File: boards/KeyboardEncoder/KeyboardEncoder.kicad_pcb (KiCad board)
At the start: 2 copper layers, 19 parts, among them J1 ISP, J2 Encoder, J3 MIDI Out, J4 SelectRX, J5 MIDI In, J7 BoardCon, J8 PistonEncoder, U1 ATmega48-20P, U2 6N138

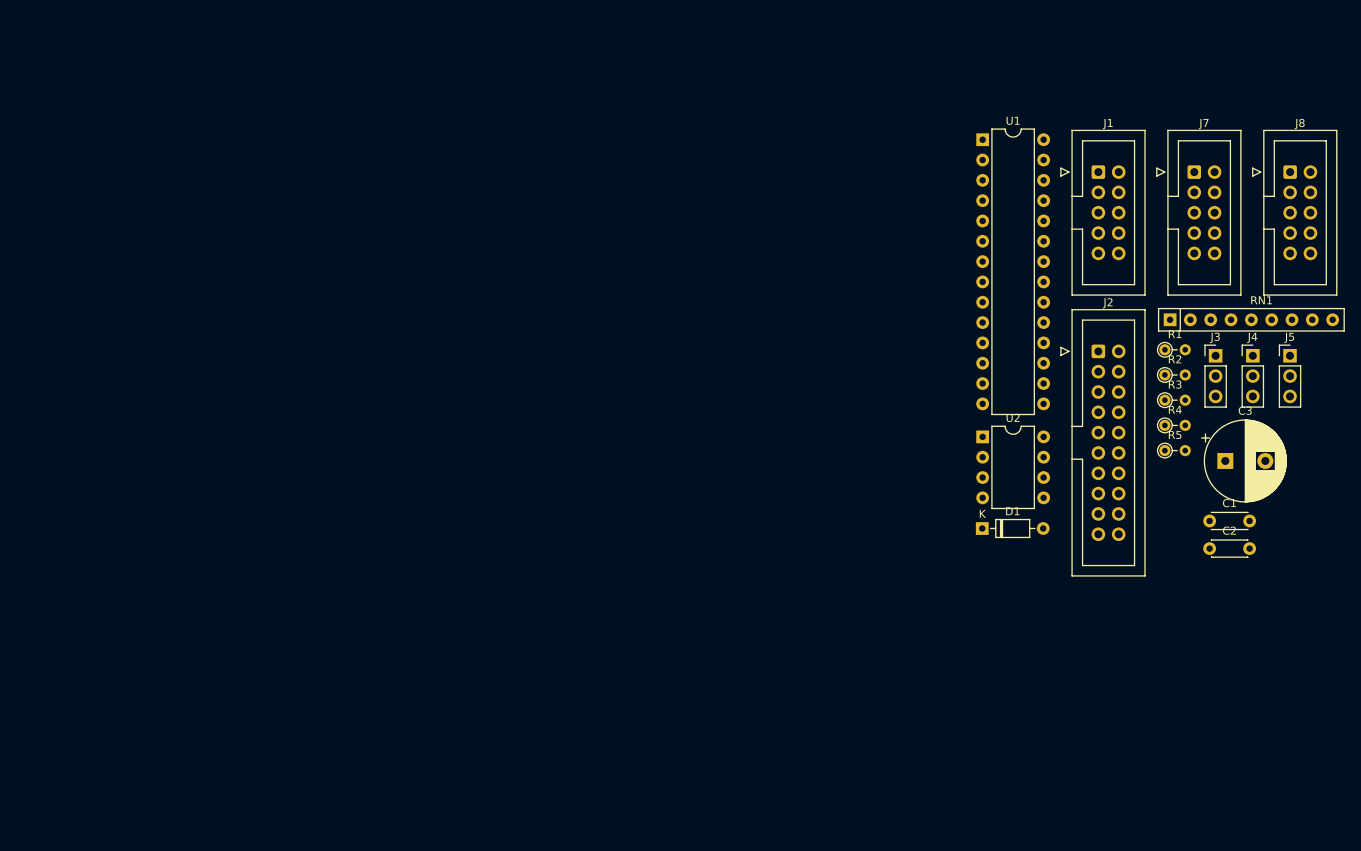
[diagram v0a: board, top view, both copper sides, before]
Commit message: Updated to KiCAD 8, fixed optocouplers for MIDI and added powersupplies
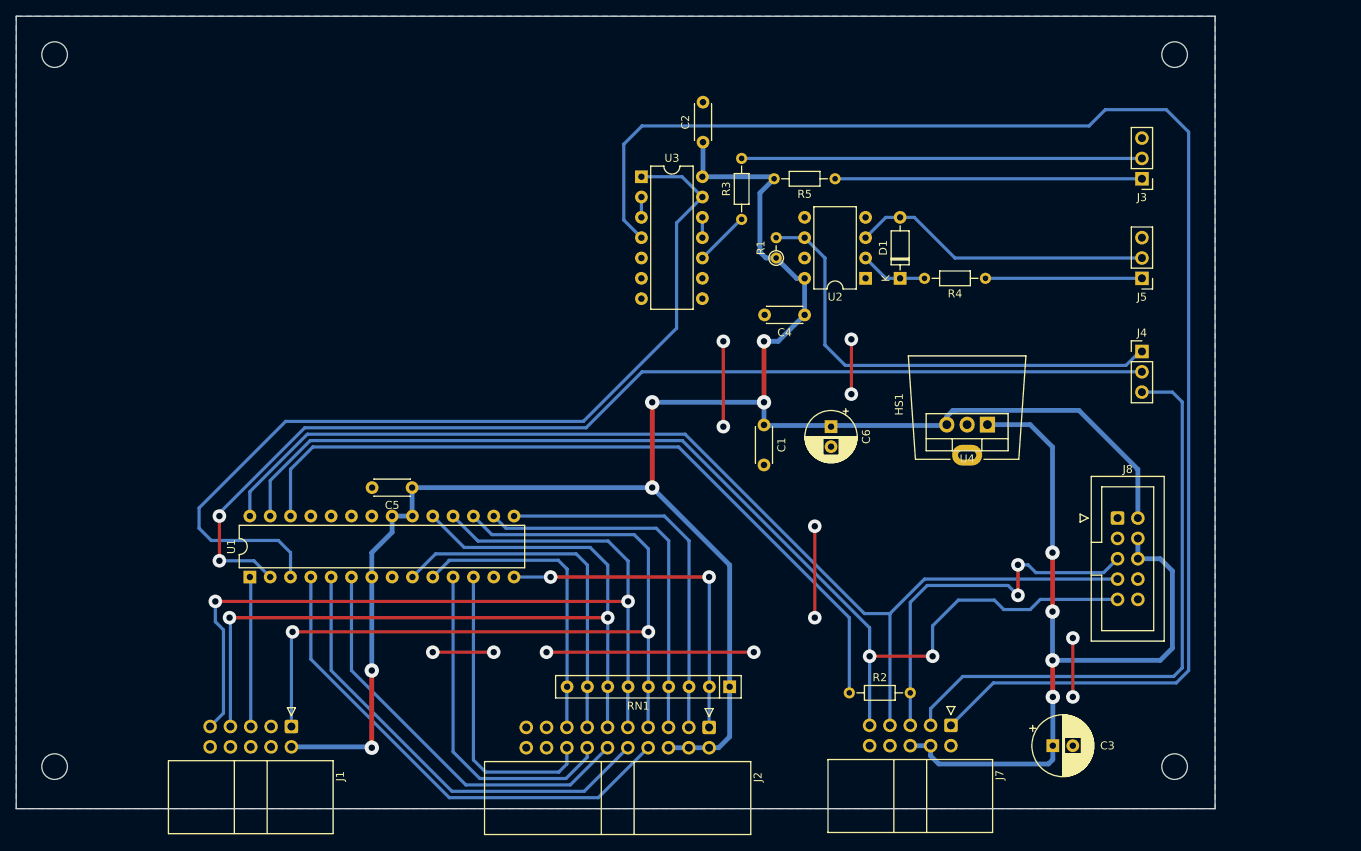
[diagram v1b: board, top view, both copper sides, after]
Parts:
- added C4: 100nF, Capacitor_THT:C_Disc_D4.3mm_W1.9mm_P5.00mm, F.Cu at (170.4, 82.5)
- added C5: 100nF, Capacitor_THT:C_Disc_D4.3mm_W1.9mm_P5.00mm, F.Cu at (121.4, 104.1)
- added C6: 10uF, Capacitor_THT:CP_Radial_D6.3mm_P2.50mm, F.Cu at (173.7, 96.5)
- added H1: MountingHole, MountingHole:MountingHole_3.2mm_M3, F.Cu at (216.7, 50.0)
- added H2: MountingHole, MountingHole:MountingHole_3.2mm_M3, F.Cu at (216.7, 139.0)
- added H3: MountingHole, MountingHole:MountingHole_3.2mm_M3, F.Cu at (76.7, 139.0)
- added H4: MountingHole, MountingHole:MountingHole_3.2mm_M3, F.Cu at (76.7, 50.0)
- added HS1: Heatsink_Pad, Heatsink:Heatsink_AAVID_576802B03900G, F.Cu at (190.7, 100.1)
- added U3: 74LS14, Package_DIP:DIP-14_W7.62mm, F.Cu at (150.0, 65.3)
- added U4: L7805, Package_TO_SOT_THT:TO-220-3_Vertical, F.Cu at (193.3, 96.3)
- C3: value C_Polarized -> 33uF; footprint Capacitor_THT:CP_Radial_D10.0mm_P5.00mm -> Capacitor_THT:CP_Radial_D7.5mm_P2.50mm
- J1, J7: footprint Connector_IDC:IDC-Header_2x05_P2.54mm_Vertical -> Connector_IDC:IDC-Header_2x05_P2.54mm_Horizontal
- J2: footprint Connector_IDC:IDC-Header_2x10_P2.54mm_Vertical -> Connector_IDC:IDC-Header_2x10_P2.54mm_Horizontal
- R1: value 10k -> 1k
- R2, R3, R4, R5: footprint Resistor_THT:R_Axial_DIN0204_L3.6mm_D1.6mm_P2.54mm_Vertical -> Resistor_THT:R_Axial_DIN0204_L3.6mm_D1.6mm_P7.62mm_Horizontal
- U2: value 6N138 -> 6N137
- moved J1 122.4 mm to (106.3, 134.0), turned to -90 degrees
- moved U1 106.7 mm to (101.1, 115.3), turned to 90 degrees
- moved C2 81.2 mm to (157.7, 61.0), turned to 90 degrees
- moved J7 75.6 mm to (188.7, 133.9), turned to -90 degrees
- moved RN1 71.7 mm to (161.1, 129.0), turned to 180 degrees
- moved J2 67.7 mm to (158.5, 134.1), turned to -90 degrees
- moved R3 57.5 mm to (162.6, 70.6), turned to 90 degrees
- moved C1 57.0 mm to (165.4, 96.3), turned to -90 degrees
- moved R2 56.0 mm to (176.0, 129.8)
- moved R5 53.4 mm to (174.2, 65.5), turned to 180 degrees
- moved R1 49.9 mm to (166.9, 75.4), turned to 90 degrees
- moved J8 48.3 mm to (209.6, 108.0)
- moved C3 41.6 mm to (201.5, 136.4)
- moved D1 32.9 mm to (182.4, 78.0), turned to 90 degrees
- moved R4 29.0 mm to (193.0, 78.0), turned to 180 degrees
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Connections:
- C3 pad 1: +5V -> +12V
- J7 pad 1: TXD -> TXT_OUT
- J7 pad 2: +5V -> unconnected-(J7-Pin_2-Pad2)
- R3 pad 1: TXD -> Net-(R3-Pad1)
- RN1 pad 2: Net-(J2-Pin_15) -> Net-(J2-Pin_1)
- RN1 pad 3: Net-(J2-Pin_13) -> Net-(J2-Pin_3)
- RN1 pad 4: SCK -> Net-(J2-Pin_5)
- RN1 pad 5: MISO -> MOSI
- RN1 pad 6: MOSI -> MISO
- RN1 pad 7: Net-(J2-Pin_5) -> SCK
- RN1 pad 8: Net-(J2-Pin_3) -> Net-(J2-Pin_13)
- RN1 pad 9: Net-(J2-Pin_1) -> Net-(J2-Pin_15)
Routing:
- net +5V: track 0.00 -> 253.2 mm, vias 0 -> 6
- net TXT_OUT: track 0.00 -> 186.0 mm
- net SDA: track 0.00 -> 140.5 mm, vias 0 -> 2
- net SCL: track 0.00 -> 139.5 mm
- net RXD: track 0.00 -> 135.8 mm, vias 0 -> 2
- net TXD: track 0.00 -> 113.7 mm
- net MISO: track 0.00 -> 113.3 mm, vias 0 -> 2
- net SCK: track 0.00 -> 105.6 mm, vias 0 -> 2
- net MOSI: track 0.00 -> 102.3 mm, vias 0 -> 2
- net +12V: track 0.00 -> 101.3 mm, vias 0 -> 4
- net Interrupt: track 0.00 -> 95.1 mm
- net Ctrl In: track 0.00 -> 74.4 mm
- net GND: track 0.00 -> 69.9 mm, vias 0 -> 12
- net S0: track 0.00 -> 62.2 mm
- net MIDI In: track 0.00 -> 59.4 mm
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- added copper zone on B.Cu, net GND
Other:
- board outline added: 149.9 x 99.1 mm

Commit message: Using custom TO220 cooler, fixed and finished several PCBs
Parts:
- HS1: footprint Heatsink:Heatsink_AAVID_576802B03900G -> Custom_Heatsinks:Heatsink_Aavid_TO-220_H12.7mm
- moved HS1 0.28 mm to (190.8, 99.8), turned to 180 degrees

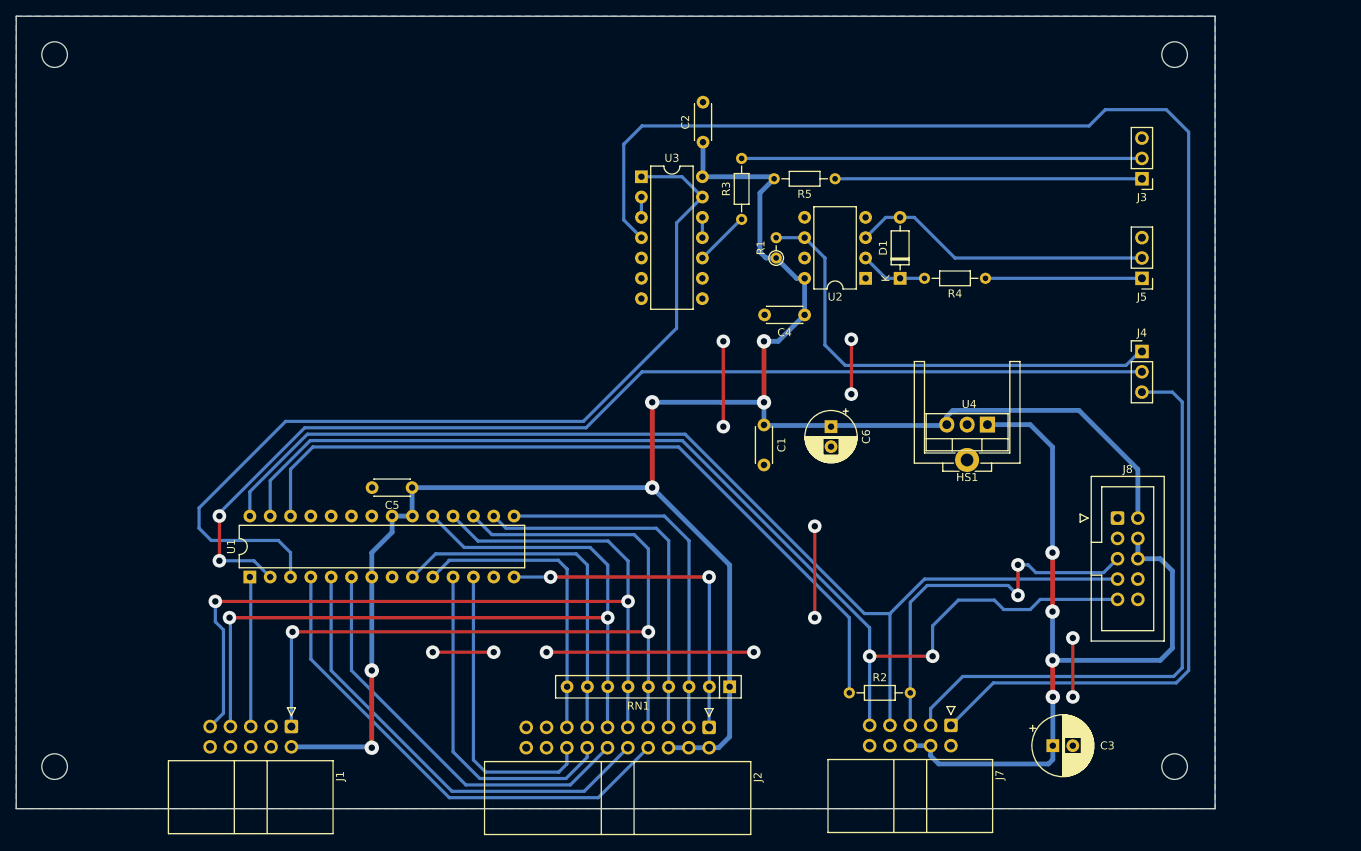
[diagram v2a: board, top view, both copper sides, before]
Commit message: Cleanup of PCB sizes and mounthole positions. Moved MIDI connectors to separate board.
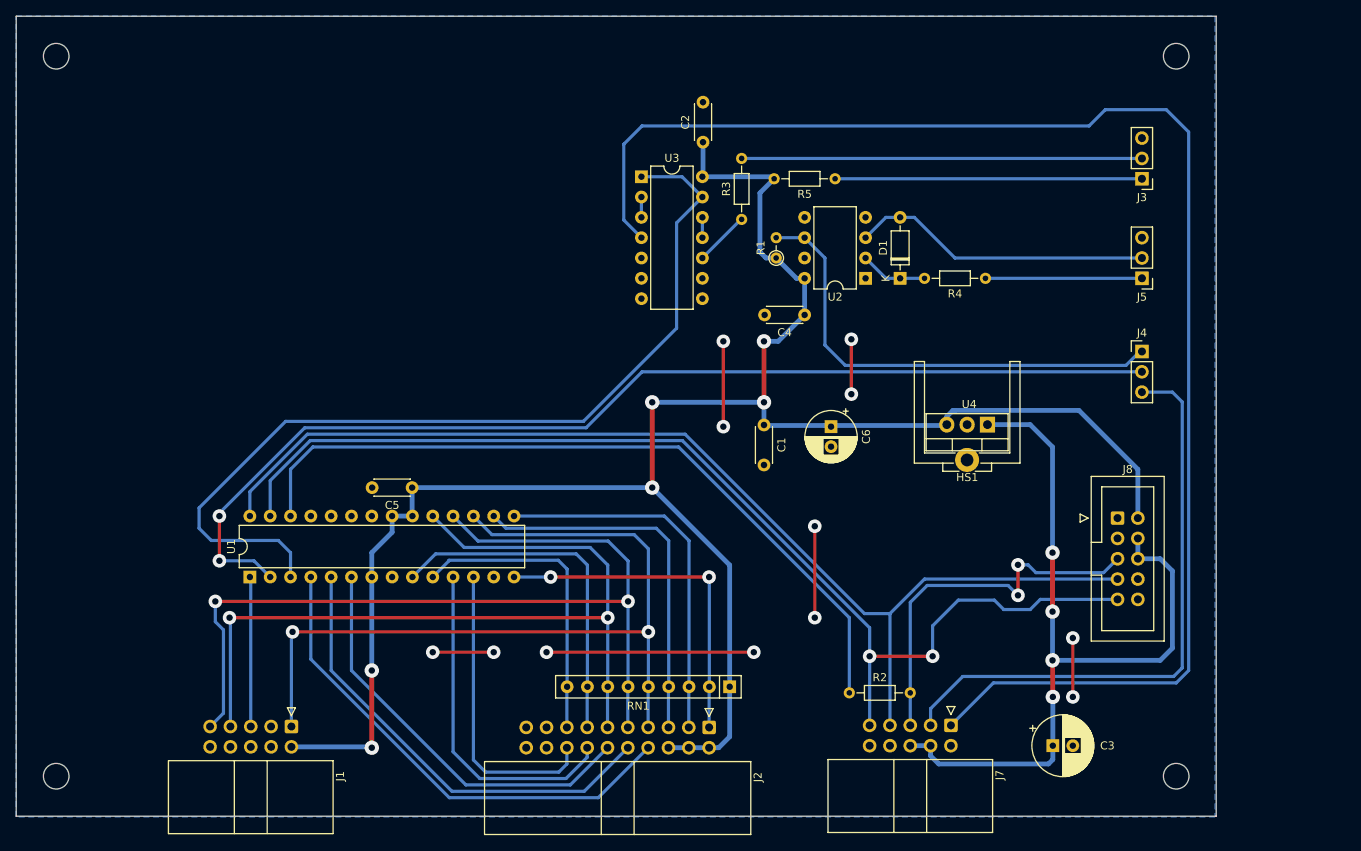
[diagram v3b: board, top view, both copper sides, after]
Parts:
- moved H2 1.22 mm to (216.9, 140.2)
- moved H3 1.22 mm to (76.9, 140.2)
- moved H1 0.28 mm to (216.9, 50.2)
- moved H4 0.28 mm to (76.9, 50.2)
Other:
- board size 149.9 x 99.1 mm -> 150 x 100 mm
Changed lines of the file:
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@@
 		(pad_to_mask_clearance 0)
 		(allow_soldermask_bridges_in_footprints no)
-		(aux_axis_origin 71.882 144.272)
+		(aux_axis_origin 71.882 45.212)
 		(pcbplotparams
 			(layerselection 0x00010fc_ffffffff)
@@
 	(footprint "MountingHole:MountingHole_3.2mm_M3"
 		(layer "F.Cu")
-		(at 216.682 139.012)
+		(at 216.882 140.212)
 		(descr "Mounting Hole 3.2mm, no annular, M3")
 		(tags "mounting hole 3.2mm no annular m3")
@@
 	(footprint "MountingHole:MountingHole_3.2mm_M3"
 		(layer "F.Cu")
-		(at 76.682 50.012)
+		(at 76.882 50.212)
 		(descr "Mounting Hole 3.2mm, no annular, M3")
 		(tags "mounting hole 3.2mm no annular m3")
@@
 	(footprint "MountingHole:MountingHole_3.2mm_M3"
 		(layer "F.Cu")
-		(at 216.682 50.012)
+		(at 216.882 50.212)
 		(descr "Mounting Hole 3.2mm, no annular, M3")
 		(tags "mounting hole 3.2mm no annular m3")
@@
 	(footprint "MountingHole:MountingHole_3.2mm_M3"
 		(layer "F.Cu")
-		(at 76.682 139.012)
+		(at 76.882 140.212)
 		(descr "Mounting Hole 3.2mm, no annular, M3")
 		(tags "mounting hole 3.2mm no annular m3")
@@
 	(gr_rect
 		(start 71.882 45.212)
-		(end 221.742 144.272)
+		(end 221.882 145.212)
 		(stroke
 			(width 0.05)
@@
 		(layer "Cmts.User")
 		(pts
-			(xy 76.682 139.572) (xy 216.682 139.572)
+			(xy 216.882 140.212) (xy 215.77 113.03)
 		)
-		(height 12.828)
-		(orientation 0)
-		(gr_text "140,0000 mm"
-			(at 146.682 150.6 0)
+		(height 10.956)
+		(orientation 1)
+		(gr_text "27,1820 mm"
+			(at 226.688 126.621 90)
 			(layer "Cmts.User")
 			(effects
 				(font
-					(size 1.5 1.5)
-					(thickness 0.3)
+					(size 1 1)
+					(thickness 0.15)
 				)
 			)
@@
 		)
 		(style
-			(thickness 0.2)
+			(thickness 0.1)
 			(arrow_length 1.27)
 			(text_position_mode 0)
@@
 		(layer "Cmts.User")
 		(pts
-			(xy 71.882 45.212) (xy 76.682 49.572)
+			(xy 76.882 140.212) (xy 216.882 140.212)
 		)
-		(height -4.064)
+		(height 12.95)
 		(orientation 0)
-		(gr_text "4,8000 mm"
-			(at 74.282 39.348 0)
+		(gr_text "140,0000 mm"
+			(at 146.882 152.012 0)
 			(layer "Cmts.User")
 			(effects
 				(font
-					(size 1.5 1.5)
-					(thickness 0.3)
+					(size 1 1)
+					(thickness 0.15)
 				)
 			)
@@
 		)
 		(style
-			(thickness 0.2)
+			(thickness 0.1)
 			(arrow_length 1.27)
 			(text_position_mode 0)
@@
 		(layer "Cmts.User")
 		(pts
-			(xy 221.742 144.272) (xy 221.742 45.212)
+			(xy 76.882 50.212) (xy 71.882 45.212)
 		)
-		(height 15.494)
-		(orientation 1)
-		(gr_text "99,0600 mm"
-			(at 235.436 94.742 90)
+		(height -9.572)
+		(orientation 0)
+		(gr_text "5,0000 mm"
+			(at 74.382 39.49 0)
 			(layer "Cmts.User")
 			(effects
 				(font
-					(size 1.5 1.5)
-					(thickness 0.3)
+					(size 1 1)
+					(thickness 0.15)
 				)
 			)
@@
 		)
 		(style
-			(thickness 0.2)
+			(thickness 0.1)
 			(arrow_length 1.27)
 			(text_position_mode 0)
@@
 		(layer "Cmts.User")
 		(pts
-			(xy 214.07 113.03) (xy 216.682 139.012)
+			(xy 71.882 45.212) (xy 76.882 50.212)
 		)
-		(height 15.8)
+		(height -4.318)
 		(orientation 1)
-		(gr_text "25,9820 mm"
-			(at 228.72 126.021 90)
+		(gr_text "5,0000 mm"
+			(at 66.414 47.712 90)
 			(layer "Cmts.User")
 			(effects
@@
 		(layer "Cmts.User")
 		(pts
-			(xy 71.882 45.212) (xy 76.682 50.012)
+			(xy 71.882 45.212) (xy 221.882 45.212)
 		)
-		(height -7.366)
-		(orientation 1)
-		(gr_text "4,8000 mm"
-			(at 62.716 47.612 90)
+		(height -9.398)
+		(orientation 0)
+		(gr_text "150,0000 mm"
+			(at 146.882 34.664 0)
 			(layer "Cmts.User")
 			(effects
 				(font
-					(size 1.5 1.5)
-					(thickness 0.3)
+					(size 1 1)
+					(thickness 0.15)
 				)
 			)
@@
 		)
 		(style
-			(thickness 0.2)
+			(thickness 0.1)
 			(arrow_length 1.27)
 			(text_position_mode 0)
@@
 		(layer "Cmts.User")
 		(pts
-			(xy 76.682 50.012) (xy 76.682 139.012)
+			(xy 71.882 144.272) (xy 146.812 144.272)
 		)
-		(height -12.166)
-		(orientation 1)
-		(gr_text "89,0000 mm"
-			(at 63.366 94.512 90)
+		(height 15.24)
+		(orientation 0)
+		(gr_text "74,9300 mm"
+			(at 109.347 157.712 0)
 			(layer "Cmts.User")
 			(effects
 				(font
-					(size 1 1)
-					(thickness 0.15)
+					(size 1.5 1.5)
+					(thickness 0.3)
 				)
 			)
@@
 		)
 		(style
-			(thickness 0.1)
+			(thickness 0.2)
 			(arrow_length 1.27)
 			(text_position_mode 0)
@@
 		(layer "Cmts.User")
 		(pts
-			(xy 221.742 45.212) (xy 71.882 45.212)
+			(xy 76.882 50.212) (xy 76.882 140.212)
 		)
-		(height -9.398)
-		(orientation 0)
-		(gr_text "149,8600 mm"
-			(at 146.812 34.014 0)
+		(height -9.572)
+		(orientation 1)
+		(gr_text "90,0000 mm"
+			(at 66.16 95.212 90)
 			(layer "Cmts.User")
 			(effects
 				(font
-					(size 1.5 1.5)
-					(thickness 0.3)
+					(size 1 1)
+					(thickness 0.15)
 				)
 			)
@@
 		)
 		(style
-			(thickness 0.2)
+			(thickness 0.1)
 			(arrow_length 1.27)
 			(text_position_mode 0)
@@
 		(layer "Cmts.User")
 		(pts
-			(xy 71.882 144.272) (xy 146.812 144.272)
+			(xy 221.882 45.212) (xy 221.882 145.212)
 		)
-		(height 15.24)
-		(orientation 0)
-		(gr_text "74,9300 mm"
-			(at 109.347 157.712 0)
+		(height 13.83)
+		(orientation 1)
+		(gr_text "100,0000 mm"
+			(at 234.562 95.212 90)
 			(layer "Cmts.User")
 			(effects
 				(font
-					(size 1.5 1.5)
-					(thickness 0.3)
+					(size 1 1)
+					(thickness 0.15)
 				)
 			)
@@
 		)
 		(style
-			(thickness 0.2)
+			(thickness 0.1)
 			(arrow_length 1.27)
 			(text_position_mode 0)
@@
 		(polygon
 			(pts
-				(xy 71.882 45.212) (xy 221.742 45.212) (xy 221.742 144.272) (xy 71.882 144.272)
+				(xy 71.882 45.212) (xy 221.742 45.212) (xy 221.742 145.288) (xy 71.882 145.288)
 			)
 		)

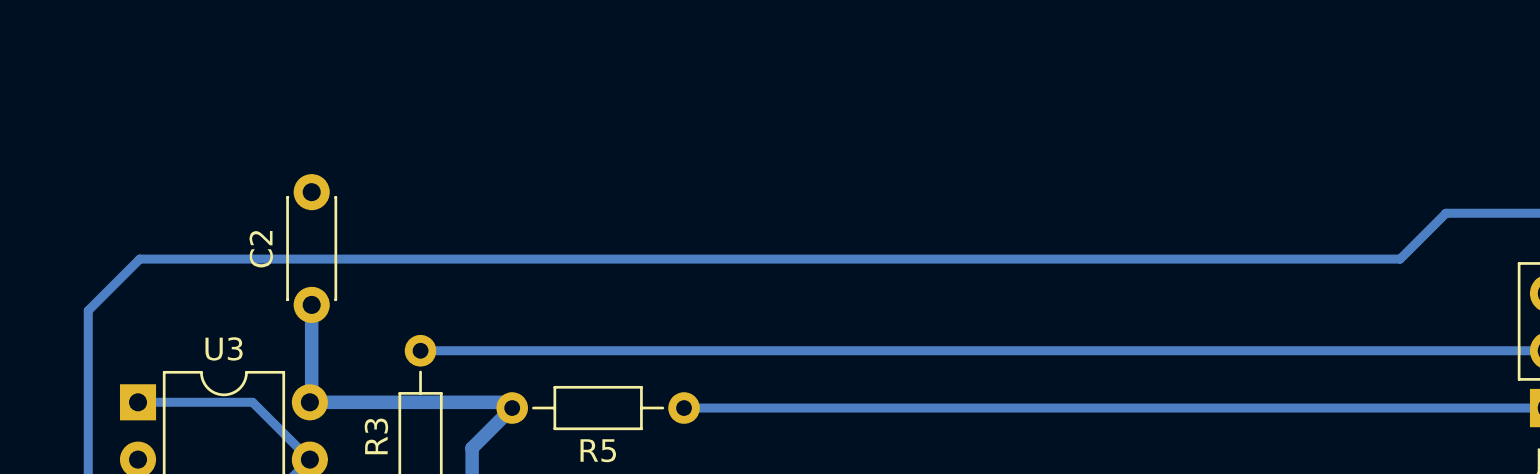
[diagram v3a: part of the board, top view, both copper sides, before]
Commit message: Added Optocoupler and RS232 converter to UART board lines.
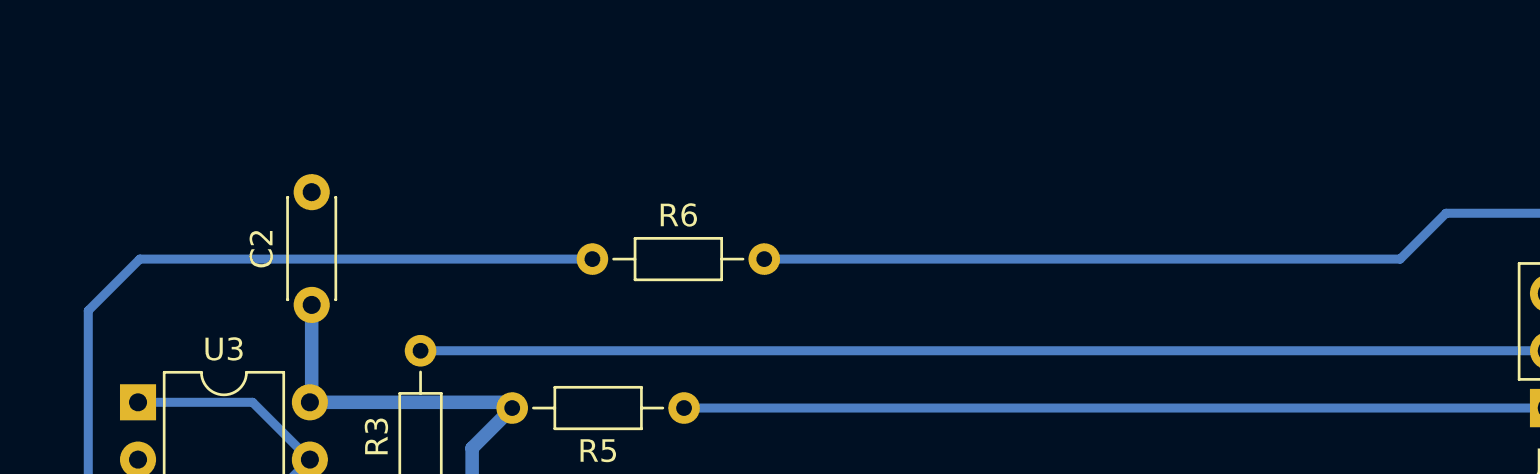
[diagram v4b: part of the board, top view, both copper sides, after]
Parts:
- added R6: 220, Resistor_THT:R_Axial_DIN0204_L3.6mm_D1.6mm_P7.62mm_Horizontal, F.Cu at (170.2, 58.9)
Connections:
- U3 pad 4: TXT_OUT -> Net-(R6-Pad1)
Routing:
- net TXT_OUT: track 186.0 -> 142.5 mm
- net Net-(R6-Pad1): track 0.00 -> 35.9 mm
